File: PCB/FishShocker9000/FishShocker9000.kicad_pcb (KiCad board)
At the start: 2 copper layers, 140 x 285.9 mm, 205 parts, among them J1 Barrel_Jack, J10 P70-1000045R, J100 P70-1000045R, J101 P70-1000045R, J102 P70-1000045R, J103 P70-1000045R, J104 P70-1000045R, J105 P70-1000045R, J106 P70-1000045R, J107 P70-1000045R, J108 P70-1000045R, J109 P70-1000045R, J11 P70-1000045R, J110 P70-1000045R, J111 P70-1000045R, J112 P70-1000045R, J113 P70-1000045R, J114 P70-1000045R, J115 P70-1000045R, J116 P70-1000045R, J117 P70-1000045R, J118 P70-1000045R, J119 P70-1000045R, J12 P70-1000045R, J120 P70-1000045R, J121 P70-1000045R, J122 P70-1000045R, J123 P70-1000045R, J124 P70-1000045R, J125 P70-1000045R, J126 P70-1000045R, J127 P70-1000045R, J128 P70-1000045R, J129 P70-1000045R, J13 P70-1000045R, J130 P70-1000045R, J131 P70-1000045R, J132 P70-1000045R, J133 P70-1000045R, J134 P70-1000045R, J135 P70-1000045R, J136 P70-1000045R, J137 P70-1000045R, J138 P70-1000045R, J139 P70-1000045R, J14 P70-1000045R, J140 P70-1000045R, J141 P70-1000045R, J142 P70-1000045R, J143 P70-1000045R, J144 P70-1000045R, J145 P70-1000045R, J15 P70-1000045R, J16 P70-1000045R, J17 P70-1000045R, J18 P70-1000045R, J19 P70-1000045R, J2 P70-1000045R, J20 P70-1000045R, J21 P70-1000045R, J22 P70-1000045R, J23 P70-1000045R, J24 P70-1000045R, J25 P70-1000045R, J26 P70-1000045R, J27 P70-1000045R, J28 P70-1000045R, J29 P70-1000045R, J3 P70-1000045R, J30 P70-1000045R, J31 P70-1000045R, J32 P70-1000045R, J33 P70-1000045R, J34 P70-1000045R, J35 P70-1000045R, J36 P70-1000045R, J37 P70-1000045R, J38 P70-1000045R, J39 P70-1000045R, J4 P70-1000045R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

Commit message: Routed all plates. Messy, gonna try and reroute to be neater
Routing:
- net Plate 11.2: track 93.8 -> 478.4 mm, vias 1 -> 2
- net Plate 11.1: track 101.9 -> 472.4 mm, vias 1 -> 2
- net Plate 10.1: track 79.5 -> 369.8 mm, vias 1 -> 2
- net Plate 8.1: track 65.0 -> 351.9 mm, vias 1 -> 2
- net Plate 12.1: track 90.5 -> 376.2 mm, vias 1 -> 2
- net Plate 10.2: track 87.8 -> 343.9 mm, vias 1 -> 2
- net Plate 8.2: track 73.6 -> 328.6 mm, vias 1 -> 2
- net Plate 12.2: track 100.8 -> 351.5 mm, vias 1 -> 2
- net Plate 9.1: track 86.5 -> 325.4 mm, vias 1 -> 2
- net Plate 5.1: track 58.5 -> 296.5 mm, vias 1 -> 2
- net Plate 7.1: track 72.0 -> 278.2 mm, vias 1 -> 4
- net Plate 6.1: track 50.7 -> 255.6 mm, vias 1 -> 2
- net Plate 9.2: track 76.3 -> 280.0 mm, vias 1 -> 2
- net Plate 4.1: track 36.2 -> 222.5 mm, vias 1 -> 4
- net Plate 5.2: track 47.5 -> 231.6 mm, vias 1 -> 2
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
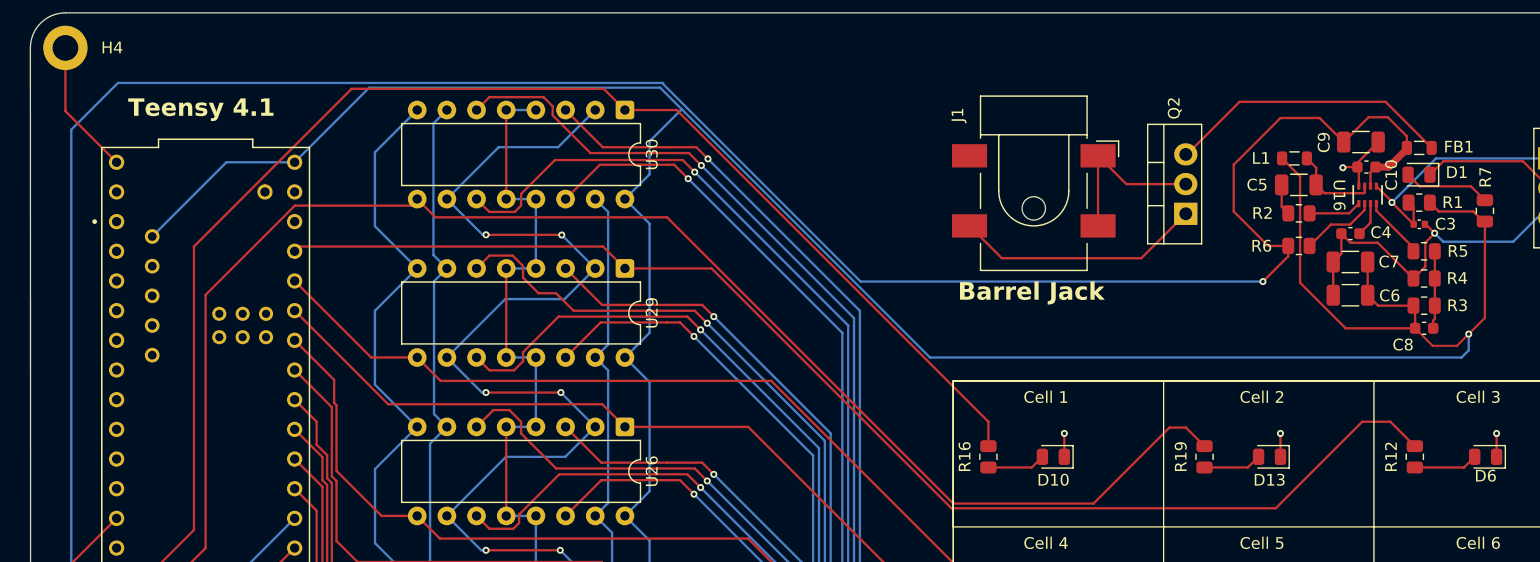
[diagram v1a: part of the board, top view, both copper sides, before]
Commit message: Fixed Teensy being double powered
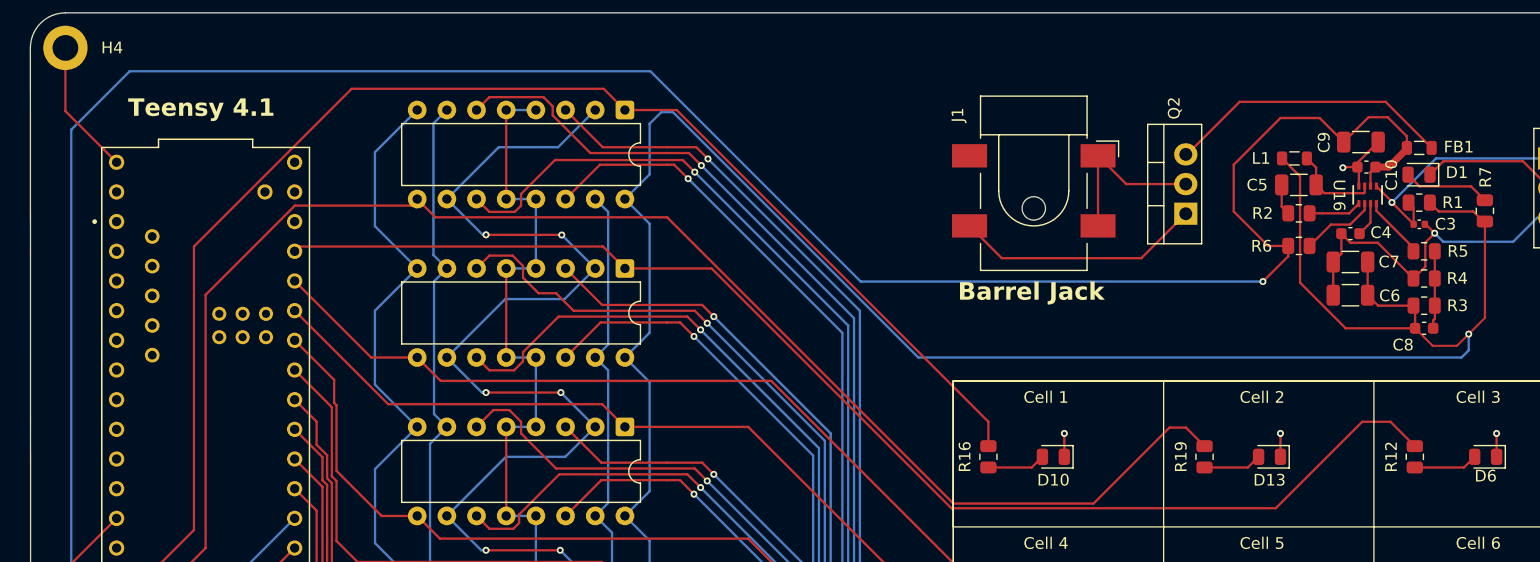
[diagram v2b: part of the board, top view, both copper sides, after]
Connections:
- U3 pad 5V: BUCK_VOUT -> unconnected-(U3-Pad5V)
- U3 pad VIN: BUCK_VOUT -> unconnected-(U3-PadVIN)
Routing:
- net BUCK_VOUT: track 309.4 -> 258.7 mm
- net BUCK_IN: track 253.8 -> 254.7 mm
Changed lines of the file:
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@@
 	(net 112 "unconnected-(U3-CRX3-Pad30)")
 	(net 113 "unconnected-(U3-CTX3-Pad31)")
+	(net 114 "unconnected-(U3-Pad5V)")
+	(net 115 "unconnected-(U3-PadVIN)")
 	(footprint "Library:HARWIN_P70-1000045R"
 		(layer "F.Cu")
@@
 			(at 3.81 -2.33 90)
 			(layer "F.SilkS")
+			(hide yes)
 			(effects
 				(font
@@
 			(at 3.81 -2.33 90)
 			(layer "F.SilkS")
+			(hide yes)
 			(effects
 				(font
@@
 			(at 3.81 -2.33 90)
 			(layer "F.SilkS")
+			(hide yes)
 			(effects
 				(font
@@
 			(layers "*.Cu" "*.Mask")
 			(remove_unused_layers no)
-			(net 5 "BUCK_VOUT")
+			(net 114 "unconnected-(U3-Pad5V)")
 			(pinfunction "5V")
-			(pintype "power_in")
+			(pintype "power_in+no_connect")
 			(solder_mask_margin 0.102)
 		)
@@
 			(layers "*.Cu" "*.Mask")
 			(remove_unused_layers no)
-			(net 5 "BUCK_VOUT")
+			(net 115 "unconnected-(U3-PadVIN)")
 			(pinfunction "VIN")
-			(pintype "input")
+			(pintype "input+no_connect")
 			(solder_mask_margin 0.102)
 		)
@@
 	)
 	(segment
-		(start 321.5 119.949)
-		(end 319.39 122.059)
+		(start 344.5 108.5)
+		(end 323.5 87.5)
 		(width 0.2)
 		(layer "B.Cu")
@@
 	)
 	(segment
-		(start 322.401 85.401)
-		(end 297.509 85.401)
+		(start 323.5 87.5)
+		(end 322.5 87.5)
 		(width 0.2)
 		(layer "B.Cu")
@@
 	)
 	(segment
-		(start 391.614099 107.885901)
-		(end 391.614099 106.494099)
+		(start 321.5 119.949)
+		(end 319.39 122.059)
 		(width 0.2)
 		(layer "B.Cu")
@@
 	)
 	(segment
-		(start 321.5 92.827)
-		(end 321.5 90)
+		(start 321.5 106.388)
+		(end 319.39 108.498)
 		(width 0.2)
 		(layer "B.Cu")
@@
 	)
 	(segment
-		(start 321.5 106.388)
-		(end 319.39 108.498)
+		(start 322.5 87.5)
+		(end 321.5 88.5)
 		(width 0.2)
 		(layer "B.Cu")
@@
 	)
 	(segment
-		(start 324.25 87.25)
-		(end 322.401 85.401)
+		(start 391.614099 107.885901)
+		(end 391 108.5)
 		(width 0.2)
 		(layer "B.Cu")
@@
 	)
 	(segment
-		(start 291.12 91.79)
-		(end 285.28 91.79)
-		(width 0.2)
-		(layer "B.Cu")
-		(net 5)
-	)
-	(segment
 		(start 321.5 97.047)
 		(end 321.5 106.388)
@@
 	)
 	(segment
-		(start 345.5 108.5)
-		(end 391 108.5)
-		(width 0.2)
-		(layer "B.Cu")
-		(net 5)
-	)
-	(segment
 		(start 284.5 164.5)
 		(end 317.205 164.5)
@@
 	)
 	(segment
-		(start 285.28 91.79)
-		(end 278.93 98.14)
-		(width 0.2)
-		(layer "B.Cu")
-		(net 5)
-	)
-	(segment
-		(start 324.25 87.25)
-		(end 345.5 108.5)
+		(start 317.205 164.5)
+		(end 319.39 162.315)
 		(width 0.2)
 		(layer "B.Cu")
@@
 	)
 	(segment
-		(start 317.205 164.5)
-		(end 319.39 162.315)
+		(start 391.614099 106.494099)
+		(end 391.614099 107.885901)
 		(width 0.2)
 		(layer "B.Cu")
@@
 	)
 	(segment
-		(start 391 108.5)
-		(end 391.614099 107.885901)
-		(width 0.2)
-		(layer "B.Cu")
-		(net 5)
-	)
-	(segment
 		(start 319.39 135.62)
 		(end 321.5 137.73)
@@
 	)
 	(segment
-		(start 297.509 85.401)
-		(end 291.12 91.79)
+		(start 321.5 124.169)
+		(end 321.5 133.51)
 		(width 0.2)
 		(layer "B.Cu")
@@
 	)
 	(segment
-		(start 321.5 124.169)
-		(end 321.5 133.51)
+		(start 321.5 92.827)
+		(end 319.39 94.937)
 		(width 0.2)
 		(layer "B.Cu")
@@
 	)
 	(segment
-		(start 321.5 90)
-		(end 324.25 87.25)
+		(start 321.5 88.5)
+		(end 321.5 92.827)
 		(width 0.2)
 		(layer "B.Cu")
@@
 	)
 	(segment
-		(start 321.5 147.071)
-		(end 319.39 149.181)
+		(start 391 108.5)
+		(end 344.5 108.5)
 		(width 0.2)
 		(layer "B.Cu")
@@
 	)
 	(segment
-		(start 319.39 94.937)
-		(end 321.5 92.827)
+		(start 321.5 147.071)
+		(end 319.39 149.181)
 		(width 0.2)
 		(layer "B.Cu")
@@
 	)
 	(segment
-		(start 295.5 163)
-		(end 295.5 161.5)
+		(start 339.5671 102)
+		(end 321.5671 84)
 		(width 0.2)
 		(layer "B.Cu")
@@
 	)
 	(segment
-		(start 273.5 164)
-		(end 294.5 164)
+		(start 294.5 164)
+		(end 295.5 163)
 		(width 0.2)
 		(layer "B.Cu")
@@
 	)
 	(segment
-		(start 272 89)
-		(end 272 162.5)
+		(start 277 84)
+		(end 272 89)
 		(width 0.2)
 		(layer "B.Cu")
@@
 	)
 	(segment
-		(start 322.6661 85)
-		(end 276 85)
+		(start 272 89)
+		(end 272 162.5)
 		(width 0.2)
 		(layer "B.Cu")
@@
 	)
 	(segment
-		(start 294.5 164)
-		(end 295.5 163)
+		(start 321.5671 84)
+		(end 277 84)
 		(width 0.2)
 		(layer "B.Cu")
@@
 	)
 	(segment
-		(start 276 85)
-		(end 272 89)
+		(start 273.5 164)
+		(end 294.5 164)
 		(width 0.2)
 		(layer "B.Cu")
@@
 	)
 	(segment
-		(start 322.6661 85.099)
-		(end 339.5671 102)
+		(start 272 162.5)
+		(end 273.5 164)
 		(width 0.2)
 		(layer "B.Cu")
@@
 	)
 	(segment
-		(start 295.5 161.5)
-		(end 294.5 160.5)
+		(start 374 102)
+		(end 339.5671 102)
 		(width 0.2)
 		(layer "B.Cu")
@@
 	)
 	(segment
-		(start 272 162.5)
-		(end 273.5 164)
+		(start 295.5 163)
+		(end 295.5 161.5)
 		(width 0.2)
 		(layer "B.Cu")
@@
 	)
 	(segment
-		(start 339.5671 102)
-		(end 374 102)
+		(start 295.5 161.5)
+		(end 294.5 160.5)
 		(width 0.2)
 		(layer "B.Cu")

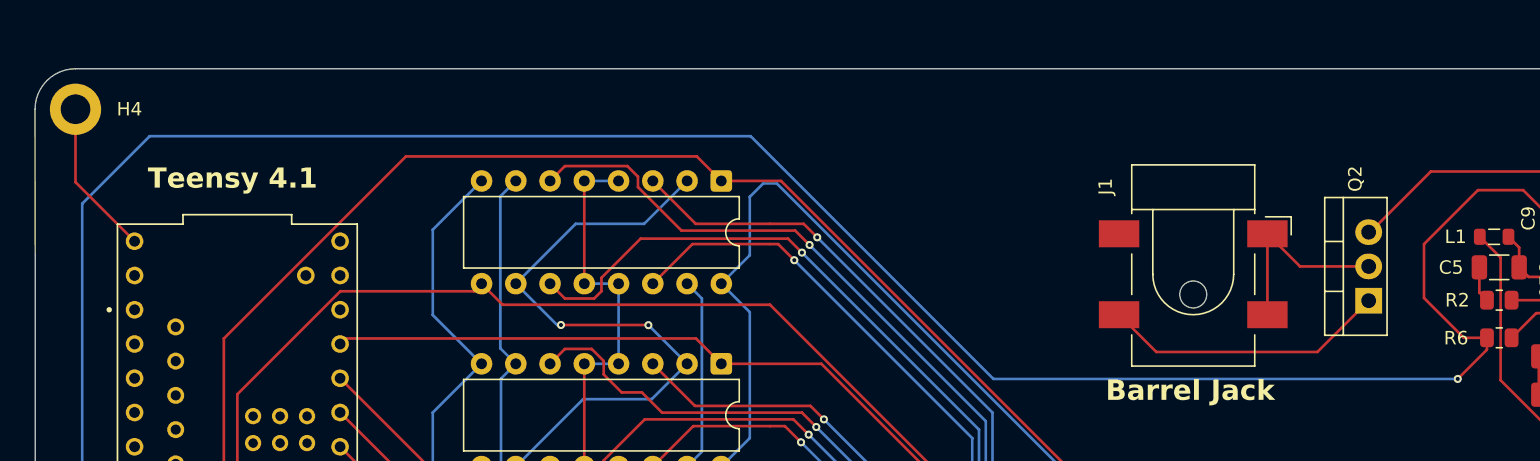
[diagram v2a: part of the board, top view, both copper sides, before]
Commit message: Added testing headers
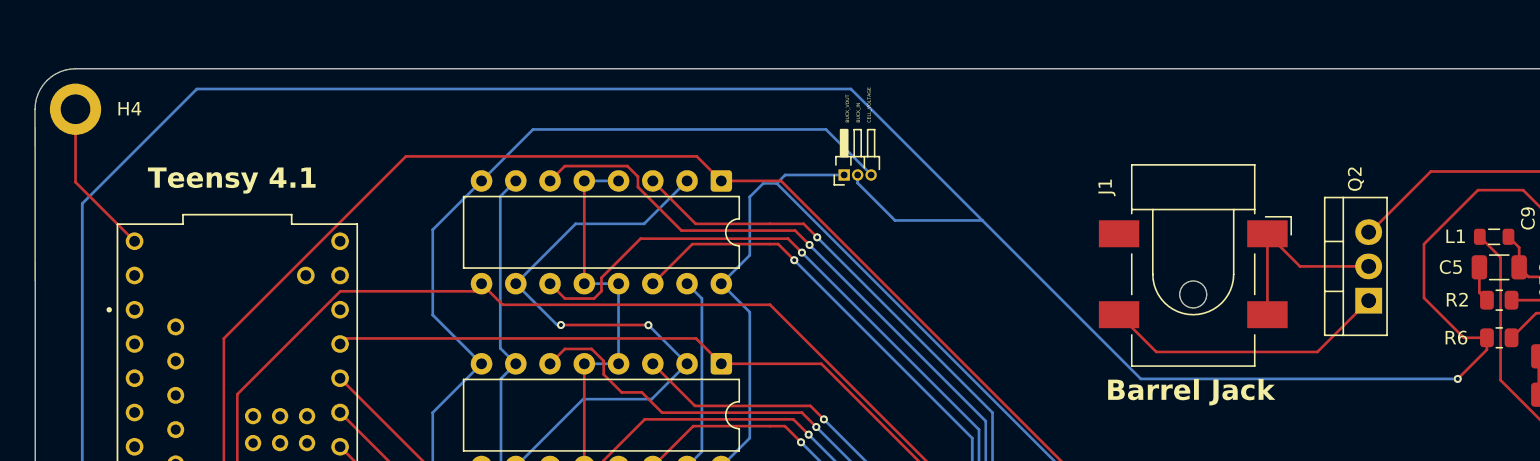
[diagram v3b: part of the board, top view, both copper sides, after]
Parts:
- added J146: Conn_01x03_Pin, Connector_PinHeader_1.00mm:PinHeader_1x03_P1.00mm_Horizontal, F.Cu at (328.5, 86.9)
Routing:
- net CELL_VOLTAGE: track 97.8 -> 129.6 mm
- net BUCK_IN: track 254.7 -> 268.6 mm
- net BUCK_VOUT: track 258.7 -> 264.0 mm
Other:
- board text added: "BUCK_VOUT BUCK_IN CELL_VOLTAGE"

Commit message: removed USB gnd
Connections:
- U3 pad USB_GND1: GND -> unconnected-(U3-USB_GND-PadUSB_GND1)_1
- U3 pad USB_GND2: GND -> unconnected-(U3-USB_GND-PadUSB_GND1)
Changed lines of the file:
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@@
 	(net 114 "unconnected-(U3-Pad5V)")
 	(net 115 "unconnected-(U3-PadVIN)")
+	(net 116 "unconnected-(U3-USB_GND-PadUSB_GND1)")
+	(net 117 "unconnected-(U3-USB_GND-PadUSB_GND1)_1")
 	(footprint "Library:HARWIN_P70-1000045R"
 		(layer "F.Cu")
@@
 			(layers "*.Cu" "*.Mask")
 			(remove_unused_layers no)
-			(net 110 "GND")
+			(net 117 "unconnected-(U3-USB_GND-PadUSB_GND1)_1")
 			(pinfunction "USB_GND")
-			(pintype "power_in")
+			(pintype "power_in+no_connect")
 			(solder_mask_margin 0.102)
 		)
@@
 			(layers "*.Cu" "*.Mask")
 			(remove_unused_layers no)
-			(net 110 "GND")
+			(net 116 "unconnected-(U3-USB_GND-PadUSB_GND1)")
 			(pinfunction "USB_GND")
-			(pintype "power_in")
+			(pintype "power_in+no_connect")
 			(solder_mask_margin 0.102)
 		)
